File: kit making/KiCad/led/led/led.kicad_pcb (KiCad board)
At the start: 2 copper layers, 17 x 17 mm, 3 parts

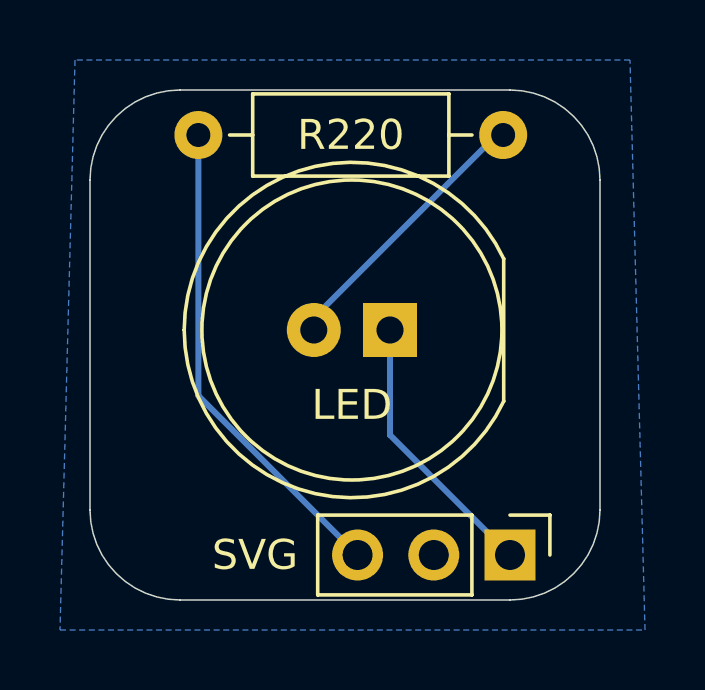
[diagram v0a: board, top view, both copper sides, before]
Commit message: Worksheet updates, box inserts, updated controller code
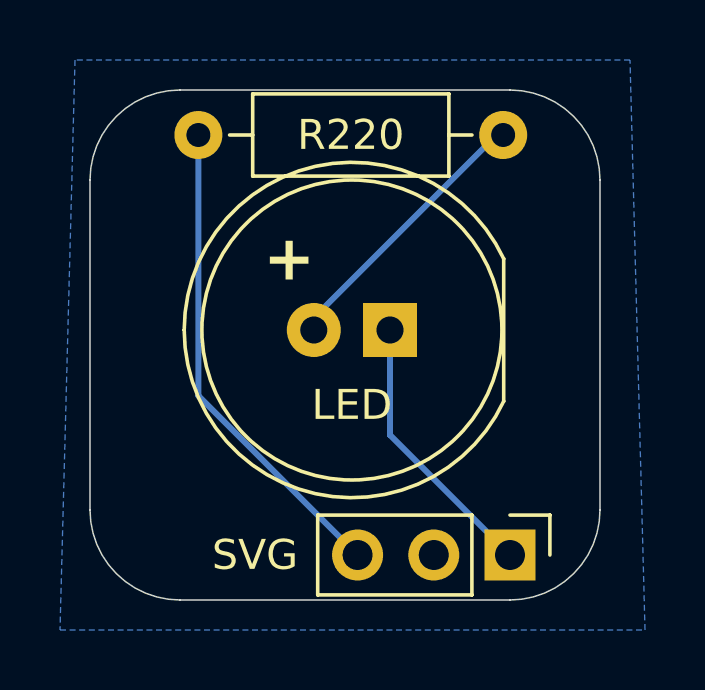
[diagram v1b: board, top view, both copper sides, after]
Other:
- board text added: "+"
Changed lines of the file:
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@@
 		(layer "Edge.Cuts")
+	)
+	(gr_text "+"
+		(at 104.5 53.5 0)
+		(layer "F.SilkS")
+		(effects
+			(font
+				(size 1.5 1.5)
+				(thickness 0.3)
+				(bold yes)
+			)
+			(justify left bottom mirror)
+		)
 	)
 	(segment
